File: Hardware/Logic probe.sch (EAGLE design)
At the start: 19 parts, among them IC1 74HC00, J1 GND_connector, Q1 BC847B

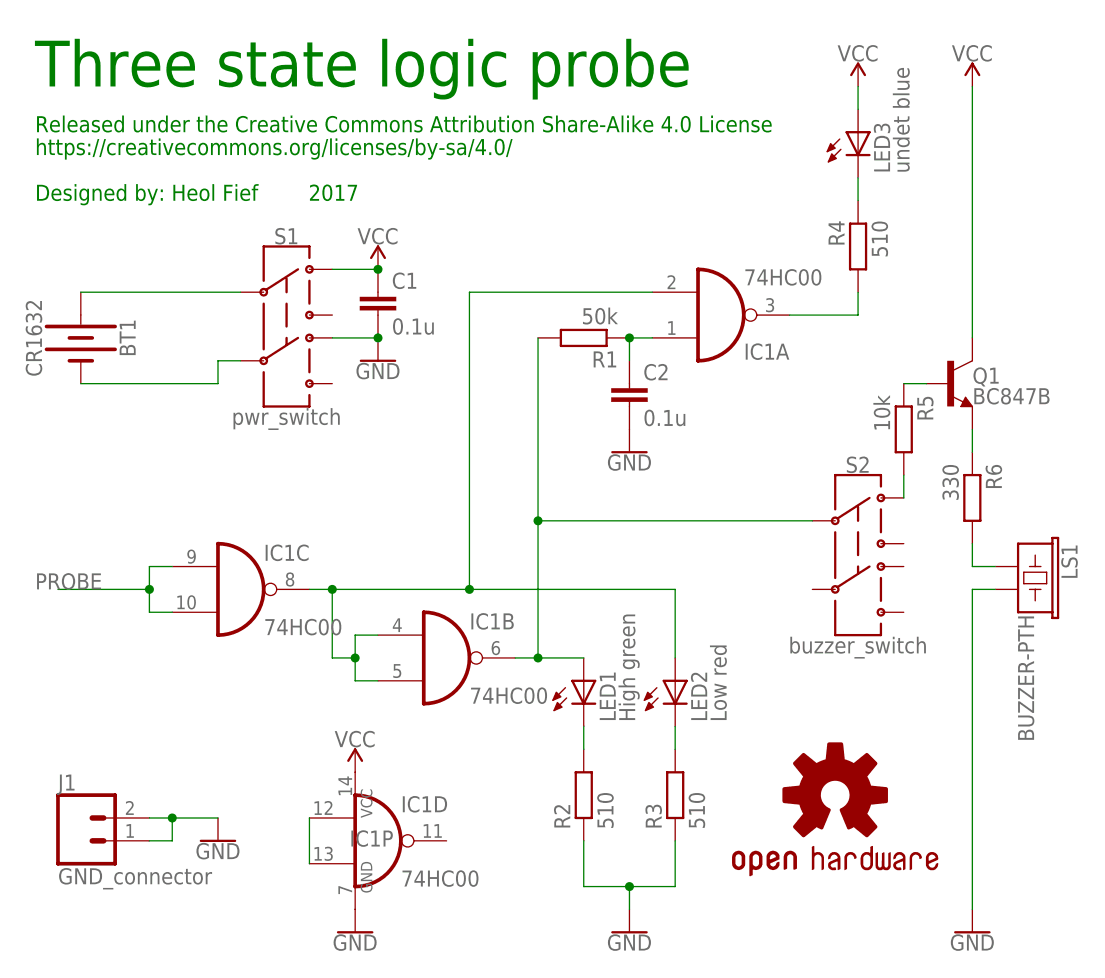
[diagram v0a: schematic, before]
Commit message: Add files via upload
Fix buzzer circuit
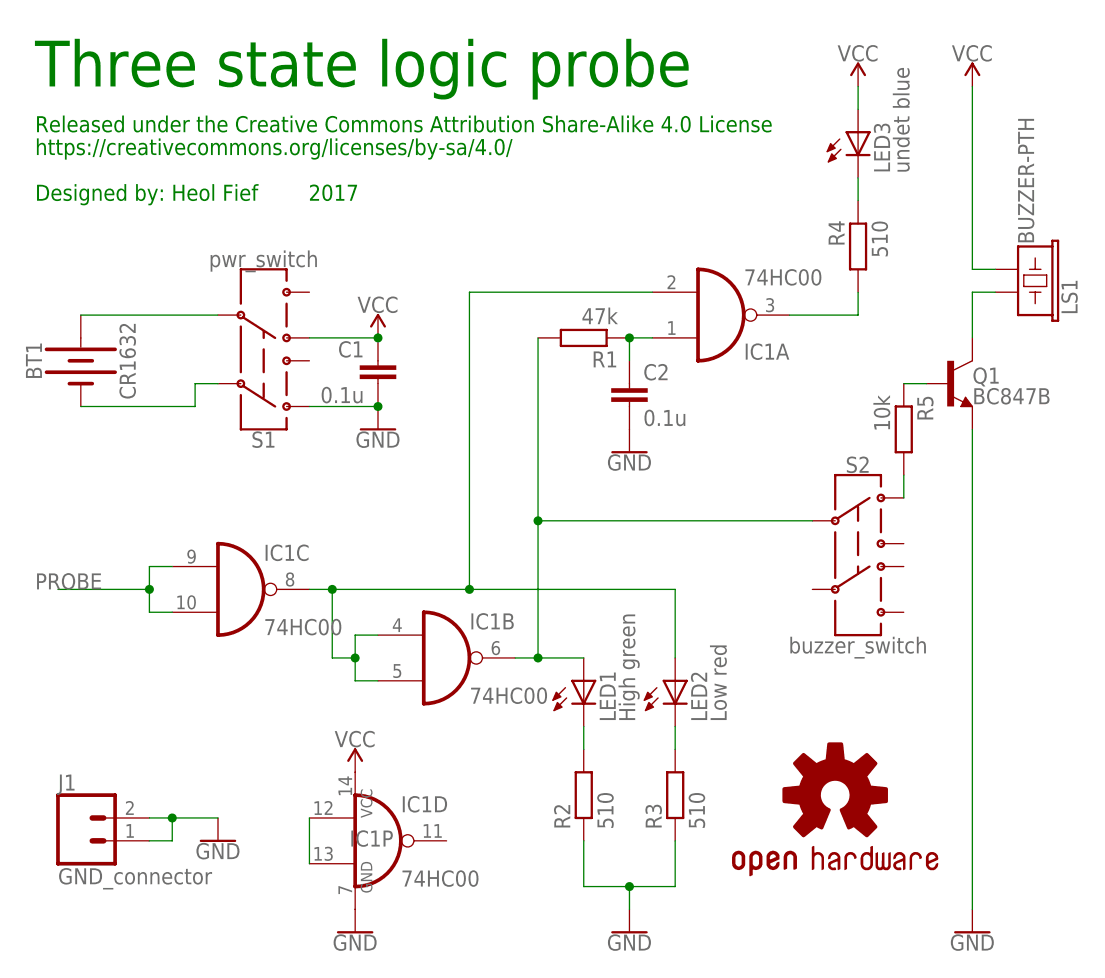
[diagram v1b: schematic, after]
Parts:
- removed R6: 330, resistor:R-EU_R1206
- R1: value 50k -> 47k
- R5: device resistor:R-EU_R1206 -> resistor:R-EU_R0805
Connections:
- removed net N$11: BT1.+, S1.2
- net GND: now also Q1.E, S1.1; no longer LS1.2, S1.4
- net N$12: now also BT1.+; no longer BT1.-
- net N$5: now also LS1.1, Q1.C; no longer Q1.E, R6.1
- net N$6: now also BT1.-, S1.2; no longer LS1.1, R6.2
- net VCC: now also LS1.2, S1.4; no longer Q1.C, S1.1
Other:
- moved on the sheet: BT1, C1, LS1, S1
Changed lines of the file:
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@@
 <part name="GND5" library="SparkFun-PowerSymbols" deviceset="GND" device=""/>
 <part name="S2" library="SparkFun-Switches" deviceset="SWITCH-DPDT" device="-SMD-AYZ0202" value="buzzer_switch"/>
-<part name="R6" library="resistor" deviceset="R-EU_" device="R1206" value="330"/>
 <part name="Q1" library="SparkFun-DiscreteSemi" deviceset="TRANS_NPN" device="-MMBT2222AL" value="BC847B"/>
-<part name="R5" library="resistor" deviceset="R-EU_" device="R1206" value="10k"/>
+<part name="R5" library="resistor" deviceset="R-EU_" device="R0805" value="10k"/>
 <part name="SUPPLY2" library="SparkFun-PowerSymbols" deviceset="VCC" device=""/>
 <part name="GND3" library="SparkFun-PowerSymbols" deviceset="GND" device=""/>
@@
 <part name="GND2" library="SparkFun-PowerSymbols" deviceset="GND" device=""/>
 <part name="BT1" library="SparkFun-Batteries" deviceset="BATTERY" device="-12MM_PTH" value="CR1632"/>
-<part name="R1" library="resistor" deviceset="R-EU_" device="R1206" value="50k"/>
+<part name="R1" library="resistor" deviceset="R-EU_" device="R1206" value="47k"/>
 <part name="C2" library="rcl" deviceset="C-EU" device="C0805" value="0.1u"/>
 <part name="GND4" library="SparkFun-PowerSymbols" deviceset="GND" device=""/>
@@
 <instance part="GND5" gate="1" x="68.58" y="2.54"/>
 <instance part="S2" gate="G$1" x="93.98" y="45.72"/>
-<instance part="R6" gate="G$1" x="106.68" y="50.8" rot="R270"/>
 <instance part="Q1" gate="G$1" x="104.14" y="63.5"/>
 <instance part="R5" gate="G$1" x="99.06" y="58.42" rot="R270"/>
-<instance part="SUPPLY2" gate="G$1" x="40.64" y="76.2"/>
-<instance part="GND3" gate="1" x="40.64" y="66.04"/>
-<instance part="S1" gate="G$1" x="30.48" y="71.12"/>
+<instance part="SUPPLY2" gate="G$1" x="40.64" y="68.58" rot="MR0"/>
+<instance part="GND3" gate="1" x="40.64" y="58.42" rot="MR0"/>
+<instance part="S1" gate="G$1" x="27.94" y="66.04" rot="MR180"/>
 <instance part="J1" gate="G$1" x="7.62" y="12.7"/>
 <instance part="GND1" gate="1" x="22.86" y="12.7"/>
@@
 </instance>
 <instance part="GND2" gate="1" x="38.1" y="2.54"/>
-<instance part="BT1" gate="G$1" x="7.62" y="68.58" rot="R270"/>
+<instance part="BT1" gate="G$1" x="7.62" y="66.04" rot="MR270"/>
 <instance part="R1" gate="G$1" x="63.5" y="68.58" rot="R180"/>
 <instance part="C2" gate="G$1" x="68.58" y="63.5"/>
 <instance part="GND4" gate="1" x="68.58" y="55.88"/>
-<instance part="LS1" gate="G$1" x="111.76" y="43.18" rot="R270"/>
-<instance part="C1" gate="G$1" x="40.64" y="73.66"/>
+<instance part="LS1" gate="G$1" x="111.76" y="73.66" rot="MR90"/>
+<instance part="C1" gate="G$1" x="40.64" y="66.04" rot="MR0"/>
 <instance part="LOGO1" gate="G$1" x="91.44" y="17.78"/>
 </instances>
@@
 <net name="VCC" class="0">
 <segment>
-<pinref part="S1" gate="G$1" pin="1"/>
 <pinref part="SUPPLY2" gate="G$1" pin="VCC"/>
-<wire x1="35.56" y1="76.2" x2="40.64" y2="76.2" width="0.1524" layer="91"/>
 <pinref part="C1" gate="G$1" pin="1"/>
-<junction x="40.64" y="76.2"/>
-</segment>
-<segment>
-<pinref part="Q1" gate="G$1" pin="C"/>
-<wire x1="106.68" y1="96.52" x2="106.68" y2="68.58" width="0.1524" layer="91"/>
-<pinref part="SUPPLY4" gate="G$1" pin="VCC"/>
+<pinref part="S1" gate="G$1" pin="4"/>
+<wire x1="33.02" y1="68.58" x2="40.64" y2="68.58" width="0.1524" layer="91"/>
+<junction x="40.64" y="68.58"/>
 </segment>
 <segment>
@@
 <pinref part="IC1" gate="P" pin="VCC"/>
 <pinref part="SUPPLY1" gate="G$1" pin="VCC"/>
+</segment>
+<segment>
+<pinref part="SUPPLY4" gate="G$1" pin="VCC"/>
+<wire x1="106.68" y1="96.52" x2="106.68" y2="76.2" width="0.1524" layer="91"/>
+<pinref part="LS1" gate="G$1" pin="2"/>
+<wire x1="106.68" y1="76.2" x2="109.22" y2="76.2" width="0.1524" layer="91"/>
 </segment>
 </net>
@@
 </segment>
 <segment>
-<pinref part="S1" gate="G$1" pin="4"/>
 <pinref part="GND3" gate="1" pin="GND"/>
-<wire x1="35.56" y1="68.58" x2="40.64" y2="68.58" width="0.1524" layer="91"/>
 <pinref part="C1" gate="G$1" pin="2"/>
-<junction x="40.64" y="68.58"/>
+<pinref part="S1" gate="G$1" pin="1"/>
+<wire x1="33.02" y1="60.96" x2="40.64" y2="60.96" width="0.1524" layer="91"/>
+<junction x="40.64" y="60.96"/>
 </segment>
 <segment>
@@
 </segment>
 <segment>
-<wire x1="106.68" y1="40.64" x2="109.22" y2="40.64" width="0.1524" layer="91"/>
-<wire x1="106.68" y1="5.08" x2="106.68" y2="40.64" width="0.1524" layer="91"/>
+<wire x1="106.68" y1="5.08" x2="106.68" y2="58.42" width="0.1524" layer="91"/>
 <pinref part="GND6" gate="1" pin="GND"/>
-<pinref part="LS1" gate="G$1" pin="2"/>
+<pinref part="Q1" gate="G$1" pin="E"/>
 </segment>
 <segment>
@@
 </segment>
 </net>
-<net name="N$5" class="0">
-<segment>
-<pinref part="Q1" gate="G$1" pin="E"/>
-<pinref part="R6" gate="G$1" pin="1"/>
-<wire x1="106.68" y1="58.42" x2="106.68" y2="55.88" width="0.1524" layer="91"/>
-</segment>
-</net>
-<net name="N$6" class="0">
-<segment>
-<pinref part="R6" gate="G$1" pin="2"/>
-<wire x1="106.68" y1="45.72" x2="106.68" y2="43.18" width="0.1524" layer="91"/>
-<wire x1="106.68" y1="43.18" x2="109.22" y2="43.18" width="0.1524" layer="91"/>
-<pinref part="LS1" gate="G$1" pin="1"/>
-</segment>
-</net>
-<net name="N$11" class="0">
-<segment>
-<wire x1="7.62" y1="73.66" x2="25.4" y2="73.66" width="0.1524" layer="91"/>
-<pinref part="S1" gate="G$1" pin="2"/>
+<net name="N$12" class="0">
+<segment>
+<pinref part="S1" gate="G$1" pin="5"/>
 <pinref part="BT1" gate="G$1" pin="+"/>
-</segment>
-</net>
-<net name="N$12" class="0">
-<segment>
-<wire x1="7.62" y1="63.5" x2="22.86" y2="63.5" width="0.1524" layer="91"/>
-<wire x1="22.86" y1="63.5" x2="22.86" y2="66.04" width="0.1524" layer="91"/>
-<pinref part="S1" gate="G$1" pin="5"/>
-<wire x1="22.86" y1="66.04" x2="25.4" y2="66.04" width="0.1524" layer="91"/>
-<pinref part="BT1" gate="G$1" pin="-"/>
+<wire x1="7.62" y1="71.12" x2="22.86" y2="71.12" width="0.1524" layer="91"/>
 </segment>
 </net>
@@
 </segment>
 </net>
+<net name="N$5" class="0">
+<segment>
+<pinref part="LS1" gate="G$1" pin="1"/>
+<pinref part="Q1" gate="G$1" pin="C"/>
+<wire x1="109.22" y1="73.66" x2="106.68" y2="73.66" width="0.1524" layer="91"/>
+<wire x1="106.68" y1="73.66" x2="106.68" y2="68.58" width="0.1524" layer="91"/>
+</segment>
+</net>
+<net name="N$6" class="0">
+<segment>
+<pinref part="BT1" gate="G$1" pin="-"/>
+<pinref part="S1" gate="G$1" pin="2"/>
+<wire x1="7.62" y1="60.96" x2="20.32" y2="60.96" width="0.1524" layer="91"/>
+<wire x1="20.32" y1="60.96" x2="20.32" y2="63.5" width="0.1524" layer="91"/>
+<wire x1="20.32" y1="63.5" x2="22.86" y2="63.5" width="0.1524" layer="91"/>
+</segment>
+</net>

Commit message: Add files via upload
Change battery size & probe lenght
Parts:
- BT1: device SparkFun-Batteries:BATTERY-12MM_PTH -> SparkFun-Batteries:BATTERY-16MM_PTH
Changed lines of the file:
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@@
 <?xml version="1.0" encoding="utf-8"?>
 <!DOCTYPE eagle SYSTEM "eagle.dtd">
-<eagle version="8.0.0">
+<eagle version="8.0.1">
 <drawing>
 <settings>
@@
 <part name="SUPPLY1" library="SparkFun-PowerSymbols" deviceset="VCC" device=""/>
 <part name="GND2" library="SparkFun-PowerSymbols" deviceset="GND" device=""/>
-<part name="BT1" library="SparkFun-Batteries" deviceset="BATTERY" device="-12MM_PTH" value="CR1632"/>
+<part name="BT1" library="SparkFun-Batteries" deviceset="BATTERY" device="-16MM_PTH" value="CR1632"/>
 <part name="R1" library="resistor" deviceset="R-EU_" device="R1206" value="47k"/>
 <part name="C2" library="rcl" deviceset="C-EU" device="C0805" value="0.1u"/>
